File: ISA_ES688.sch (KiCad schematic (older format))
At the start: 112 parts, among them J1 ISA BUS, J2 Interrupt Select, J3 Address Select, J4 DMA Select, J5 Joystick/MIDI, J6 LINE OUT, J7 MIC, J8 LINE IN, J9 SPKR OUT, U1 74LS14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

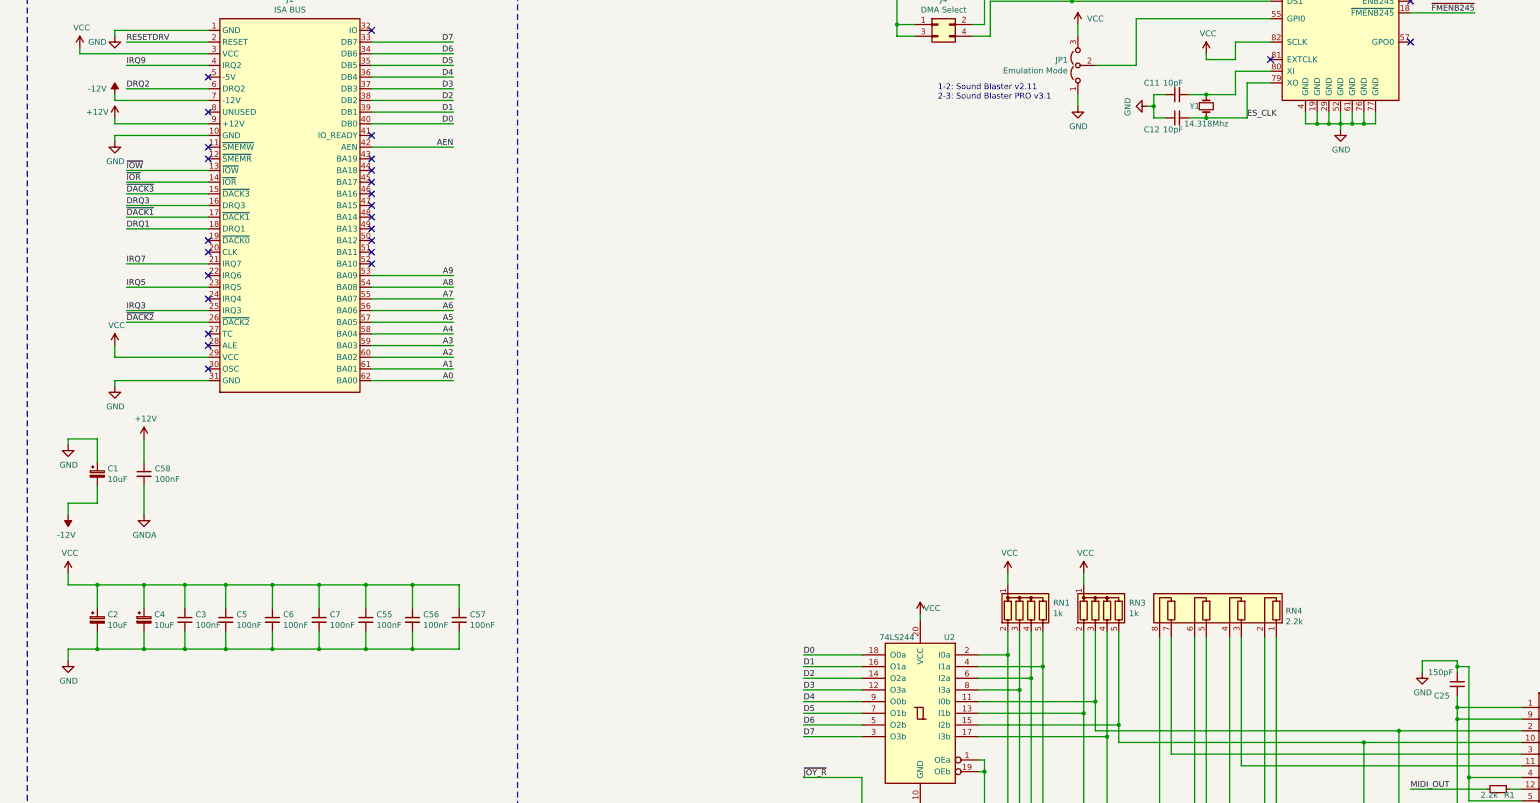
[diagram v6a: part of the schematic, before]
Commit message: Completed routing of board
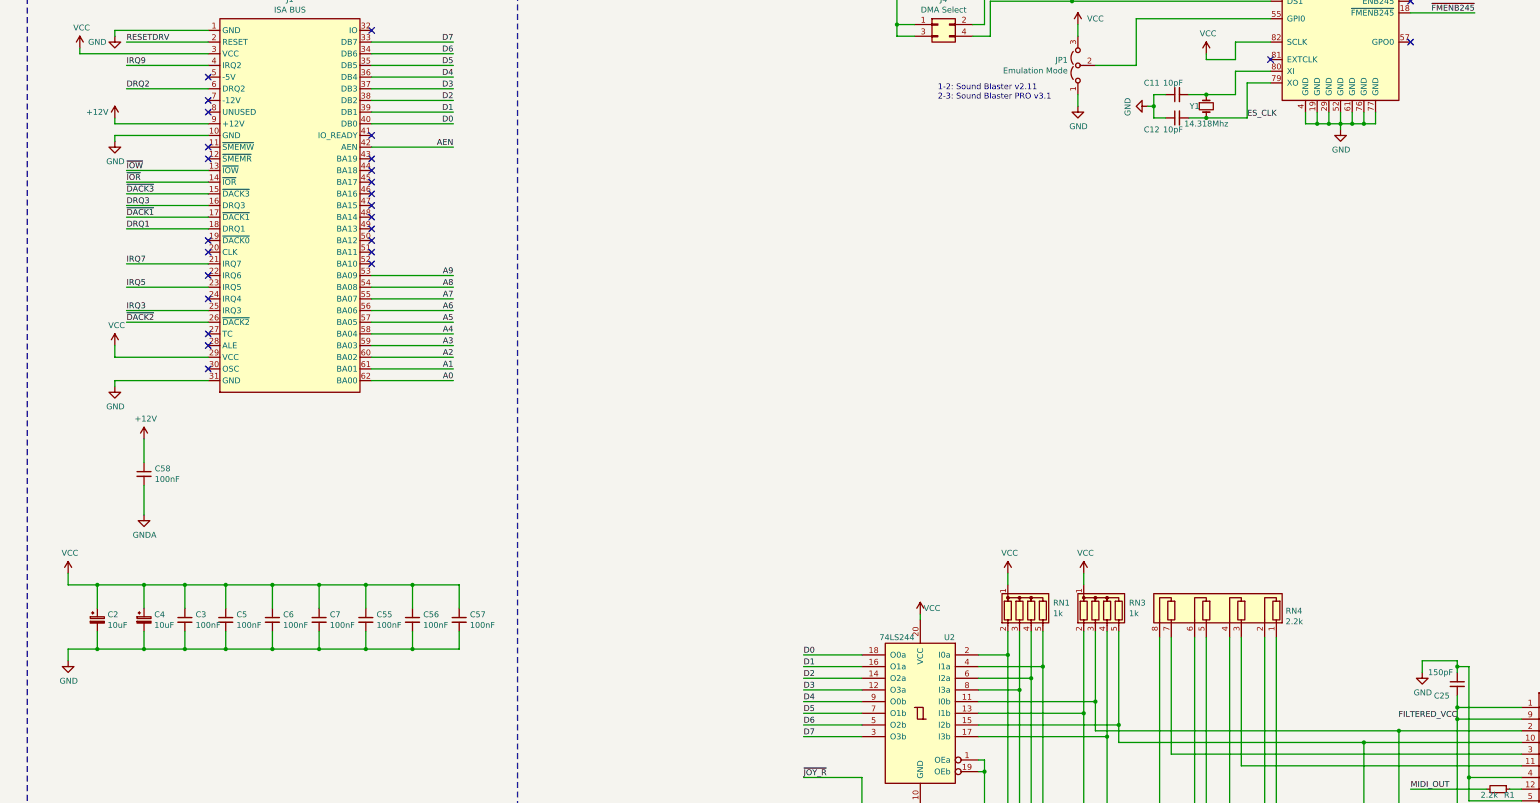
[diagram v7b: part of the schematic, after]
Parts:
- removed C1: 10uF, Capacitor_THT:CP_Radial_D5.0mm_P2.50mm, symbol Device:CP_Small
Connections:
- net FILTERED_VCC: now reaches C25.2, J5.1, J5.8, J5.9 (P9), L2.2
- net -12V: no longer names the net of J1.7 (-12V)
- no-connect marks 39 -> 40
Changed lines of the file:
@@
-$EndComp
-Wire Wire Line
-	1100 10500 1100 10600
-Wire Wire Line
-	1350 10500 1100 10500
-Wire Wire Line
-	1350 10500 1350 10350
-$Comp
-L power:-12V #PWR04
-U 1 1 610C70C1
-P 1100 10600
-F 0 "#PWR04" H 1100 10700 50  0001 C CNN
-F 1 "-12V" H 1115 10773 50  0000 C CNN
-F 2 "" H 1100 10600 50  0001 C CNN
-F 3 "" H 1100 10600 50  0001 C CNN
-	1    1100 10600
-	-1   0    0    1
-$EndComp
-Wire Wire Line
-	1350 9950 1350 10150
-Wire Wire Line
-	1100 9950 1350 9950
-Wire Wire Line
-	1100 10000 1100 9950
-$Comp
-L power:GND #PWR03
-U 1 1 6108687E
-P 1100 10000
-F 0 "#PWR03" H 1100 9750 50  0001 C CNN
-F 1 "GND" H 1105 9827 50  0000 C CNN
-F 2 "" H 1100 10000 50  0001 C CNN
-F 3 "" H 1100 10000 50  0001 C CNN
-	1    1100 10000
-	1    0    0    -1
 $EndComp
 Wire Wire Line
@@
 F 3 "" H 1500 7200 50  0001 C CNN
 	1    1500 7200
-	1    0    0    -1
-$EndComp
-Wire Wire Line
-	1500 7050 2300 7050
-Wire Wire Line
-	1500 7000 1500 7050
-$Comp
-L power:-12V #PWR09
-U 1 1 60E8203A
-P 1500 7000
-F 0 "#PWR09" H 1500 7100 50  0001 C CNN
-F 1 "-12V" H 1350 7050 50  0000 C CNN
-F 2 "" H 1500 7000 50  0001 C CNN
-F 3 "" H 1500 7000 50  0001 C CNN
-	1    1500 7000
 	1    0    0    -1
 $EndComp
@@
 $EndComp
 $Comp
-L Device:CP_Small C1
-U 1 1 610853FE
-P 1350 10250
-F 0 "C1" H 1438 10296 50  0000 L CNN
-F 1 "10uF" H 1438 10205 50  0000 L CNN
-F 2 "Capacitor_THT:CP_Radial_D5.0mm_P2.50mm" H 1350 10250 50  0001 C CNN
-F 3 "~" H 1350 10250 50  0001 C CNN
-	1    1350 10250
-	1    0    0    -1
-$EndComp
-$Comp
 L Device:Ferrite_Bead_Small L1
 U 1 1 62245E2F
@@
 Wire Wire Line
 	1750 10350 1750 10600
+NoConn ~ 2300 7050
+Text Label 13000 12350 2    50   ~ 0
+FILTERED_VCC
 $EndSCHEMATC

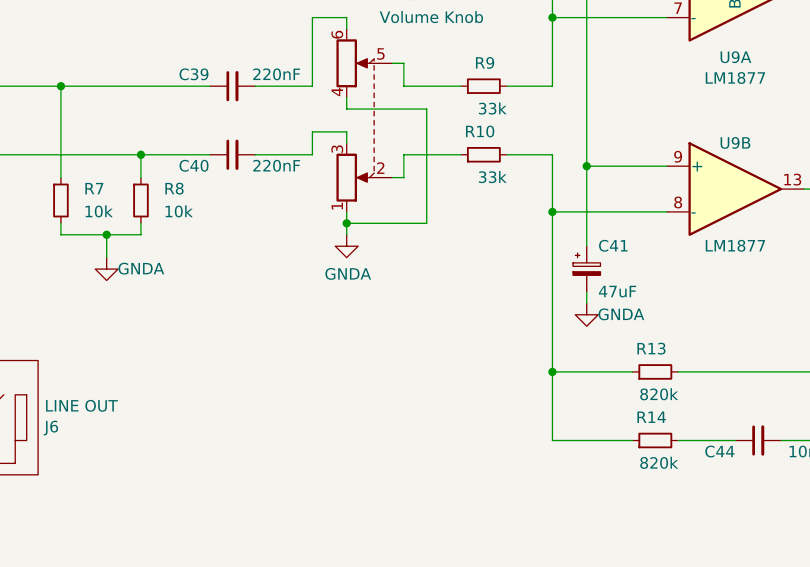
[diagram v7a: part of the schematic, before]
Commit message: Added two resistors after the volume pot
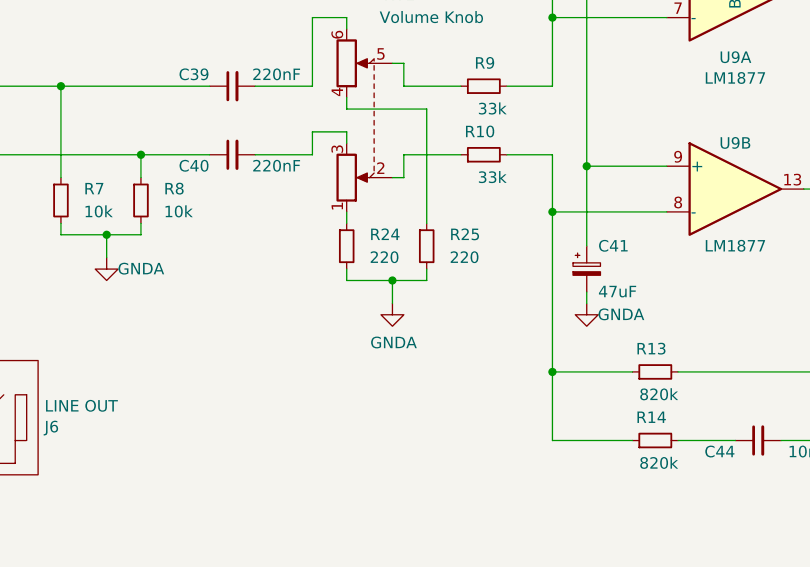
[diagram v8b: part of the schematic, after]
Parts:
- added R24, R25: 220, Resistor_SMD:R_1206_3216Metric_Pad1.30x1.75mm_HandSolder, symbol Device:R_Small
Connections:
- net GNDA: now also R24.2, R25.2; no longer RV1.1, RV1.4
- new net: R25.1, RV1.4
- new net: R24.1, RV1.1
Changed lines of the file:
@@
 L power:GNDA #PWR055
 U 1 1 6388FADA
-P 17300 4750
-F 0 "#PWR055" H 17300 4500 50  0001 C CNN
-F 1 "GNDA" H 17305 4577 50  0000 C CNN
-F 2 "" H 17300 4750 50  0001 C CNN
-F 3 "" H 17300 4750 50  0001 C CNN
-	1    17300 4750
+P 17500 5050
+F 0 "#PWR055" H 17500 4800 50  0001 C CNN
+F 1 "GNDA" H 17505 4877 50  0000 C CNN
+F 2 "" H 17500 5050 50  0001 C CNN
+F 3 "" H 17500 5050 50  0001 C CNN
+	1    17500 5050
 	1    0    0    -1
 $EndComp
@@
 	17150 3800 17300 3800
 Wire Wire Line
-	17300 4650 17300 4700
-Wire Wire Line
 	17300 4200 17650 4200
 Wire Wire Line
 	17650 4200 17650 4700
-Wire Wire Line
-	17650 4700 17300 4700
-Connection ~ 17300 4700
-Wire Wire Line
-	17300 4700 17300 4750
 Wire Wire Line
 	2100 11600 2100 11750
@@
 Text Label 13000 12350 2    50   ~ 0
 FILTERED_VCC
+$Comp
+L Device:R_Small R25
+U 1 1 60AE15A5
+P 17650 4800
+F 0 "R25" H 17750 4850 50  0000 L CNN
+F 1 "220" H 17750 4750 50  0000 L CNN
+F 2 "Resistor_SMD:R_1206_3216Metric_Pad1.30x1.75mm_HandSolder" H 17650 4800 50  0001 C CNN
+F 3 "~" H 17650 4800 50  0001 C CNN
+	1    17650 4800
+	1    0    0    -1
+$EndComp
+$Comp
+L Device:R_Small R24
+U 1 1 60AE27E3
+P 17300 4800
+F 0 "R24" H 17400 4850 50  0000 L CNN
+F 1 "220" H 17400 4750 50  0000 L CNN
+F 2 "Resistor_SMD:R_1206_3216Metric_Pad1.30x1.75mm_HandSolder" H 17300 4800 50  0001 C CNN
+F 3 "~" H 17300 4800 50  0001 C CNN
+	1    17300 4800
+	1    0    0    -1
+$EndComp
+Wire Wire Line
+	17300 4700 17300 4650
+Wire Wire Line
+	17300 4900 17300 4950
+Wire Wire Line
+	17300 4950 17500 4950
+Wire Wire Line
+	17650 4950 17650 4900
+Wire Wire Line
+	17500 5050 17500 4950
+Connection ~ 17500 4950
+Wire Wire Line
+	17500 4950 17650 4950
 $EndSCHEMATC
